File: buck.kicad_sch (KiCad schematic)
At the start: 12 parts, among them IC2 RT6285GSP

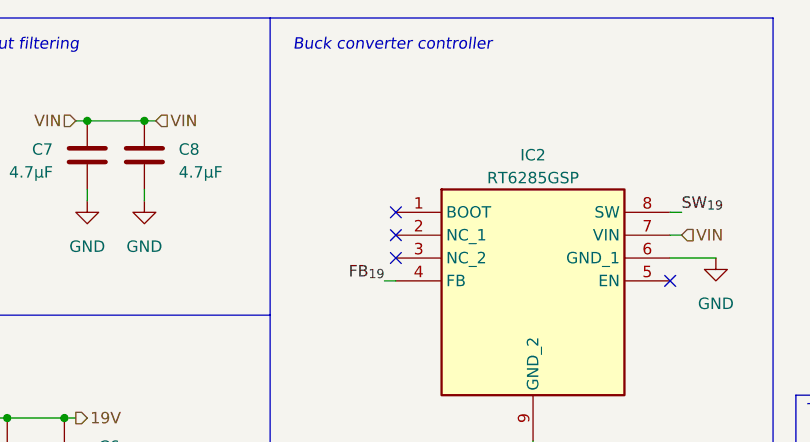
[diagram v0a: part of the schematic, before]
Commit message: Add 10nF bootstrap cap
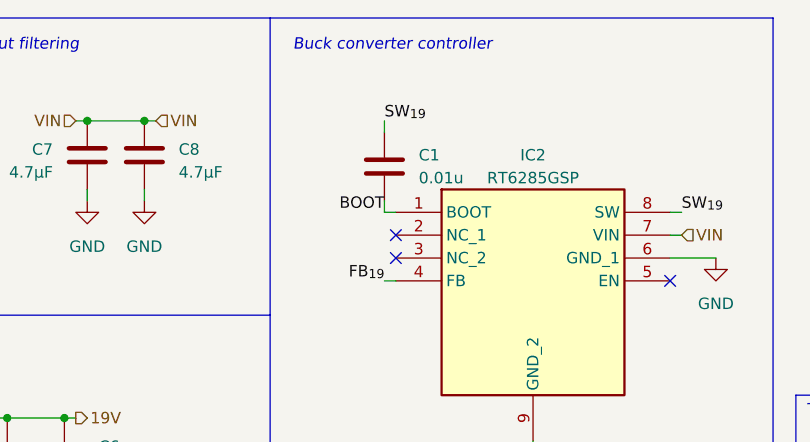
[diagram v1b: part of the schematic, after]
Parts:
- added C1: 0.01u, Capacitor_SMD:C_0603_1608Metric_Pad1.08x0.95mm_HandSolder, symbol Device:C
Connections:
- net SW_{19}: now also C1.1
- net BOOT: now reaches IC2.1 (BOOT)
- net BOOT: now also C1.2
- no-connect marks 4 -> 3
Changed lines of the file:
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@@
-	)
-	(no_connect
-		(at 132.08 67.31)
 	)
 	(no_connect
@@
 	(wire
 		(pts
+			(xy 130.81 67.31) (xy 132.08 67.31)
+		)
+		(stroke
+			(width 0)
+			(type default)
+		)
+	)
+	(wire
+		(pts
 			(xy 58.42 52.07) (xy 59.69 52.07)
 		)
@@
 		)
 	)
+	(wire
+		(pts
+			(xy 130.81 66.04) (xy 130.81 67.31)
+		)
+		(stroke
+			(width 0)
+			(type default)
+		)
+	)
 	(polyline
 		(pts
 			(xy 118.11 45.72) (xy 118.11 110.49)
+		)
+		(stroke
+			(width 0)
+			(type default)
+		)
+	)
+	(wire
+		(pts
+			(xy 130.81 57.15) (xy 130.81 58.42)
 		)
 		(stroke
@@
 		)
 	)
+	(label "SW_{19}"
+		(at 130.81 57.15 0)
+		(effects
+			(font
+				(size 1.27 1.27)
+			)
+			(justify left bottom)
+		)
+	)
 	(label "FB_{19}"
 		(at 130.81 74.93 180)
+		(effects
+			(font
+				(size 1.27 1.27)
+			)
+			(justify right bottom)
+		)
+	)
+	(label "BOOT"
+		(at 130.81 67.31 180)
 		(effects
 			(font
@@
 					(unit 1)
 				)
+			)
+		)
+	)
+	(symbol
+		(lib_id "Device:C")
+		(at 130.81 62.23 0)
+		(unit 1)
+		(exclude_from_sim no)
+		(in_bom yes)
+		(on_board yes)
+		(dnp no)
+		(property "Reference" "C1"
+			(at 134.62 60.9599 0)
+			(effects
+				(font
+					(size 1.27 1.27)
+				)
+				(justify left)
+			)
+		)
+		(property "Value" "0.01u"
+			(at 134.62 63.4999 0)
+			(effects
+				(font
+					(size 1.27 1.27)
+				)
+				(justify left)
+			)
+		)
+		(property "Footprint" "Capacitor_SMD:C_0603_1608Metric_Pad1.08x0.95mm_HandSolder"
+			(at 131.7752 66.04 0)
+			(effects
+				(font
+					(size 1.27 1.27)
+				)
+				(hide yes)
+			)
+		)
+		(property "Datasheet" "~"
+			(at 130.81 62.23 0)
+			(effects
+				(font
+					(size 1.27 1.27)
+				)
+				(hide yes)
+			)
+		)
+		(property "Description" "Unpolarized capacitor"
+			(at 130.81 62.23 0)
+			(effects
+				(font
+					(size 1.27 1.27)
+				)
+				(hide yes)
+			)
+		)
+		(pin "2"
+		)
+		(pin "1"
+		)
+		(instances
+			(project ""
+				(path "/d5f28ba3-2393-441a-9a3a-5aa9d797472a/632f64e1-f4ac-4fce-8dc1-2a6086852be0"
+					(reference "C1")
+					(unit 1)
+				)

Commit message: Staging changes
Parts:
- C1: Mouser Part Number (none) -> 710-885012204004
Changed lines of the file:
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@@
+			)
+		)
+		(property "Mouser Part Number" "710-885012204004 "
+			(at 131.064 62.23 0)
+			(effects
+				(font
+					(size 1.27 1.27)
+				)
+				(hide yes)
 			)
 		)
